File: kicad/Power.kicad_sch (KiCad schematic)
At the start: 10 parts

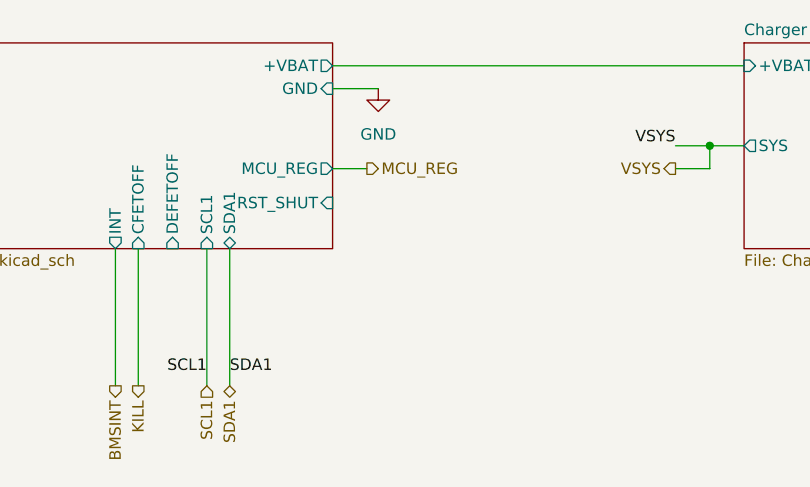
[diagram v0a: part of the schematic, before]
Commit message: Charger IC footprint routed RP2040 routed BMS routed xt30s and balancers router
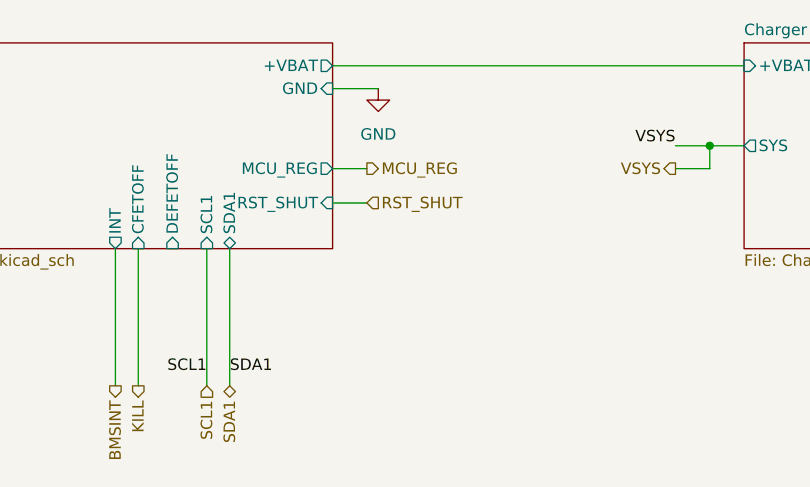
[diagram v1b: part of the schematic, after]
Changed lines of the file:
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@@
+	(wire
+		(pts
+			(xy 69.85 39.37) (xy 66.04 39.37)
+		)
+		(stroke
+			(width 0)
+			(type default)
+		)
+	)
 	(wire
 		(pts
@@
 		(effects
 			(font
+				(size 1.27 1.27)
+			)
+			(justify left)
+		)
+	)
+	(hierarchical_label "RST_SHUT"
+		(shape input)
+		(at 69.85 39.37 0)
+		(effects
+			(font
